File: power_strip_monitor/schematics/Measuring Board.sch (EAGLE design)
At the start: 3 parts, among them U1 78M6612

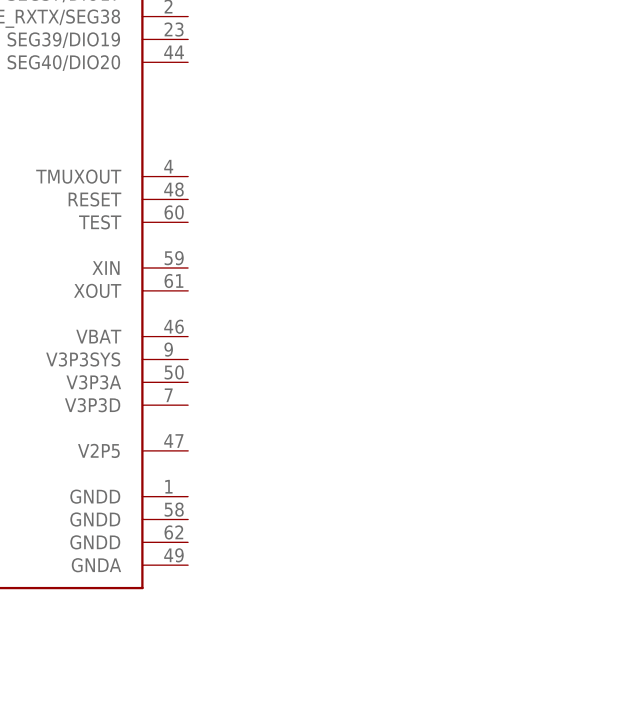
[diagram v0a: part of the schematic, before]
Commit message: Added ground/supply connections.
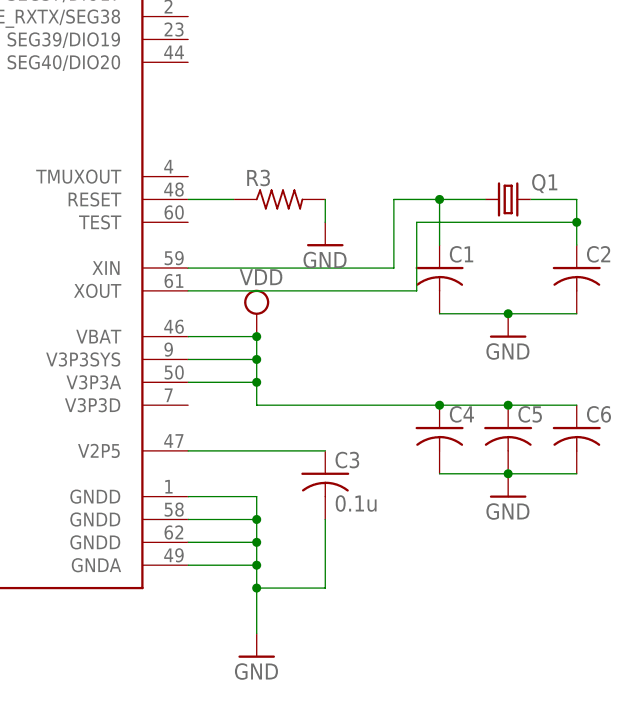
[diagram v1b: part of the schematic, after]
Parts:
- added C1, C2, C4, C5, C6: (no value), resistor:C-US025-024X044
- added C3: 0.1u, resistor:C-US025-024X044
- added Q1: (no value), crystal:CRYSTAL68SMX
- added R3: (no value), resistor:R-US_0204/2V
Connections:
- new net GND: C1.2, C2.2, C3.2, C4.2, C5.2, C6.2, R3.2, U1.GNDA, U1.GNDD@1, U1.GNDD@2, U1.GNDD@3
- new net N$1: C3.1, U1.V2P5
- new net N$5: R3.1, U1.RESET
- new net N$6: C1.1, Q1.1, U1.XIN
- new net N$7: C2.1, Q1.2, U1.XOUT
- new net VDD: C4.1, C5.1, C6.1, U1.V3P3A, U1.V3P3SYS, U1.VBAT
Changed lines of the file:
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@@
 <part name="R1" library="resistor" deviceset="R-US_" device="0204/2V"/>
 <part name="R2" library="resistor" deviceset="R-US_" device="0204/2V"/>
+<part name="GND1" library="supply1" deviceset="GND" device=""/>
+<part name="R3" library="resistor" deviceset="R-US_" device="0204/2V"/>
+<part name="GND2" library="supply1" deviceset="GND" device=""/>
+<part name="Q1" library="crystal" deviceset="CRYSTAL" device="68SMX"/>
+<part name="C1" library="resistor" deviceset="C-US" device="025-024X044"/>
+<part name="C2" library="resistor" deviceset="C-US" device="025-024X044"/>
+<part name="GND3" library="supply1" deviceset="GND" device=""/>
+<part name="C3" library="resistor" deviceset="C-US" device="025-024X044" value="0.1u"/>
+<part name="SUPPLY1" library="supply2" deviceset="VDD" device=""/>
+<part name="C4" library="resistor" deviceset="C-US" device="025-024X044"/>
+<part name="C5" library="resistor" deviceset="C-US" device="025-024X044"/>
+<part name="C6" library="resistor" deviceset="C-US" device="025-024X044"/>
+<part name="GND5" library="supply1" deviceset="GND" device=""/>
 </parts>
 <sheets>
@@
 <instance part="R1" gate="G$1" x="5.08" y="50.8"/>
 <instance part="R2" gate="G$1" x="5.08" y="35.56"/>
+<instance part="GND1" gate="1" x="170.18" y="7.62"/>
+<instance part="R3" gate="G$1" x="172.72" y="58.42"/>
+<instance part="GND2" gate="1" x="177.8" y="53.34"/>
+<instance part="Q1" gate="G$1" x="198.12" y="58.42"/>
+<instance part="C1" gate="G$1" x="190.5" y="50.8"/>
+<instance part="C2" gate="G$1" x="205.74" y="50.8"/>
+<instance part="GND3" gate="1" x="198.12" y="43.18"/>
+<instance part="C3" gate="G$1" x="177.8" y="27.94"/>
+<instance part="SUPPLY1" gate="G$1" x="170.18" y="45.72"/>
+<instance part="C4" gate="G$1" x="190.5" y="33.02"/>
+<instance part="C5" gate="G$1" x="198.12" y="33.02"/>
+<instance part="C6" gate="G$1" x="205.74" y="33.02"/>
+<instance part="GND5" gate="1" x="198.12" y="25.4"/>
 </instances>
 <busses>
@@
 </segment>
 </net>
+<net name="GND" class="0">
+<segment>
+<pinref part="U1" gate="G$1" pin="GNDA"/>
+<wire x1="162.56" y1="17.78" x2="170.18" y2="17.78" width="0.1524" layer="91"/>
+<pinref part="GND1" gate="1" pin="GND"/>
+<wire x1="170.18" y1="17.78" x2="170.18" y2="15.24" width="0.1524" layer="91"/>
+<pinref part="U1" gate="G$1" pin="GNDD@3"/>
+<wire x1="170.18" y1="15.24" x2="170.18" y2="10.16" width="0.1524" layer="91"/>
+<wire x1="162.56" y1="20.32" x2="170.18" y2="20.32" width="0.1524" layer="91"/>
+<wire x1="170.18" y1="20.32" x2="170.18" y2="17.78" width="0.1524" layer="91"/>
+<junction x="170.18" y="17.78"/>
+<pinref part="U1" gate="G$1" pin="GNDD@2"/>
+<wire x1="162.56" y1="22.86" x2="170.18" y2="22.86" width="0.1524" layer="91"/>
+<wire x1="170.18" y1="22.86" x2="170.18" y2="20.32" width="0.1524" layer="91"/>
+<junction x="170.18" y="20.32"/>
+<pinref part="U1" gate="G$1" pin="GNDD@1"/>
+<wire x1="162.56" y1="25.4" x2="170.18" y2="25.4" width="0.1524" layer="91"/>
+<wire x1="170.18" y1="25.4" x2="170.18" y2="22.86" width="0.1524" layer="91"/>
+<junction x="170.18" y="22.86"/>
+<pinref part="C3" gate="G$1" pin="2"/>
+<wire x1="177.8" y1="22.86" x2="177.8" y2="15.24" width="0.1524" layer="91"/>
+<wire x1="177.8" y1="15.24" x2="170.18" y2="15.24" width="0.1524" layer="91"/>
+<junction x="170.18" y="15.24"/>
+</segment>
+<segment>
+<pinref part="R3" gate="G$1" pin="2"/>
+<pinref part="GND2" gate="1" pin="GND"/>
+<wire x1="177.8" y1="58.42" x2="177.8" y2="55.88" width="0.1524" layer="91"/>
+</segment>
+<segment>
+<pinref part="C1" gate="G$1" pin="2"/>
+<pinref part="GND3" gate="1" pin="GND"/>
+<wire x1="198.12" y1="45.72" x2="190.5" y2="45.72" width="0.1524" layer="91"/>
+<pinref part="C2" gate="G$1" pin="2"/>
+<wire x1="198.12" y1="45.72" x2="205.74" y2="45.72" width="0.1524" layer="91"/>
+<junction x="198.12" y="45.72"/>
+</segment>
+<segment>
+<pinref part="C5" gate="G$1" pin="2"/>
+<pinref part="GND5" gate="1" pin="GND"/>
+<pinref part="C4" gate="G$1" pin="2"/>
+<wire x1="190.5" y1="27.94" x2="198.12" y2="27.94" width="0.1524" layer="91"/>
+<junction x="198.12" y="27.94"/>
+<pinref part="C6" gate="G$1" pin="2"/>
+<wire x1="198.12" y1="27.94" x2="205.74" y2="27.94" width="0.1524" layer="91"/>
+</segment>
+</net>
+<net name="N$5" class="0">
+<segment>
+<pinref part="U1" gate="G$1" pin="RESET"/>
+<pinref part="R3" gate="G$1" pin="1"/>
+<wire x1="162.56" y1="58.42" x2="167.64" y2="58.42" width="0.1524" layer="91"/>
+</segment>
+</net>
+<net name="N$6" class="0">
+<segment>
+<pinref part="U1" gate="G$1" pin="XIN"/>
+<wire x1="162.56" y1="50.8" x2="185.42" y2="50.8" width="0.1524" layer="91"/>
+<wire x1="185.42" y1="50.8" x2="185.42" y2="58.42" width="0.1524" layer="91"/>
+<pinref part="Q1" gate="G$1" pin="1"/>
+<wire x1="185.42" y1="58.42" x2="190.5" y2="58.42" width="0.1524" layer="91"/>
+<pinref part="C1" gate="G$1" pin="1"/>
+<wire x1="190.5" y1="58.42" x2="195.58" y2="58.42" width="0.1524" layer="91"/>
+<wire x1="190.5" y1="58.42" x2="190.5" y2="53.34" width="0.1524" layer="91"/>
+<junction x="190.5" y="58.42"/>
+</segment>
+</net>
+<net name="N$7" class="0">
+<segment>
+<pinref part="Q1" gate="G$1" pin="2"/>
+<wire x1="200.66" y1="58.42" x2="205.74" y2="58.42" width="0.1524" layer="91"/>
+<pinref part="C2" gate="G$1" pin="1"/>
+<wire x1="205.74" y1="58.42" x2="205.74" y2="55.88" width="0.1524" layer="91"/>
+<pinref part="U1" gate="G$1" pin="XOUT"/>
+<wire x1="205.74" y1="55.88" x2="205.74" y2="53.34" width="0.1524" layer="91"/>
+<wire x1="162.56" y1="48.26" x2="187.96" y2="48.26" width="0.1524" layer="91"/>
+<wire x1="187.96" y1="48.26" x2="187.96" y2="55.88" width="0.1524" layer="91"/>
+<wire x1="187.96" y1="55.88" x2="205.74" y2="55.88" width="0.1524" layer="91"/>
+<junction x="205.74" y="55.88"/>
+</segment>
+</net>
+<net name="N$1" class="0">
+<segment>
+<pinref part="U1" gate="G$1" pin="V2P5"/>
+<pinref part="C3" gate="G$1" pin="1"/>
+<wire x1="162.56" y1="30.48" x2="177.8" y2="30.48" width="0.1524" layer="91"/>
+</segment>
+</net>
+<net name="VDD" class="0">
+<segment>
+<pinref part="U1" gate="G$1" pin="VBAT"/>
+<pinref part="SUPPLY1" gate="G$1" pin="VDD"/>
+<wire x1="162.56" y1="43.18" x2="170.18" y2="43.18" width="0.1524" layer="91"/>
+<pinref part="U1" gate="G$1" pin="V3P3SYS"/>
+<wire x1="162.56" y1="40.64" x2="170.18" y2="40.64" width="0.1524" layer="91"/>
+<wire x1="170.18" y1="40.64" x2="170.18" y2="43.18" width="0.1524" layer="91"/>
+<junction x="170.18" y="43.18"/>
+<pinref part="U1" gate="G$1" pin="V3P3A"/>
+<wire x1="162.56" y1="38.1" x2="170.18" y2="38.1" width="0.1524" layer="91"/>
+<wire x1="170.18" y1="38.1" x2="170.18" y2="40.64" width="0.1524" layer="91"/>
+<junction x="170.18" y="40.64"/>
+<pinref part="C4" gate="G$1" pin="1"/>
+<wire x1="170.18" y1="38.1" x2="170.18" y2="35.56" width="0.1524" layer="91"/>
+<wire x1="170.18" y1="35.56" x2="190.5" y2="35.56" width="0.1524" layer="91"/>
+<junction x="170.18" y="38.1"/>
+<pinref part="C5" gate="G$1" pin="1"/>
+<wire x1="190.5" y1="35.56" x2="198.12" y2="35.56" width="0.1524" layer="91"/>
+<junction x="190.5" y="35.56"/>
+<pinref part="C6" gate="G$1" pin="1"/>
+<wire x1="198.12" y1="35.56" x2="205.74" y2="35.56" width="0.1524" layer="91"/>
+<junction x="198.12" y="35.56"/>
+</segment>
+</net>
